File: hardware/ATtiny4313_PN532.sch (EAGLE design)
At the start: 22 parts, among them IC1 ATtiny4313, J2 AVR ISP, Q1 14.7456MHz, U1 PCA9543AD,118, U3 LTC490CN8PBF, U4 LTC490CN8PBF

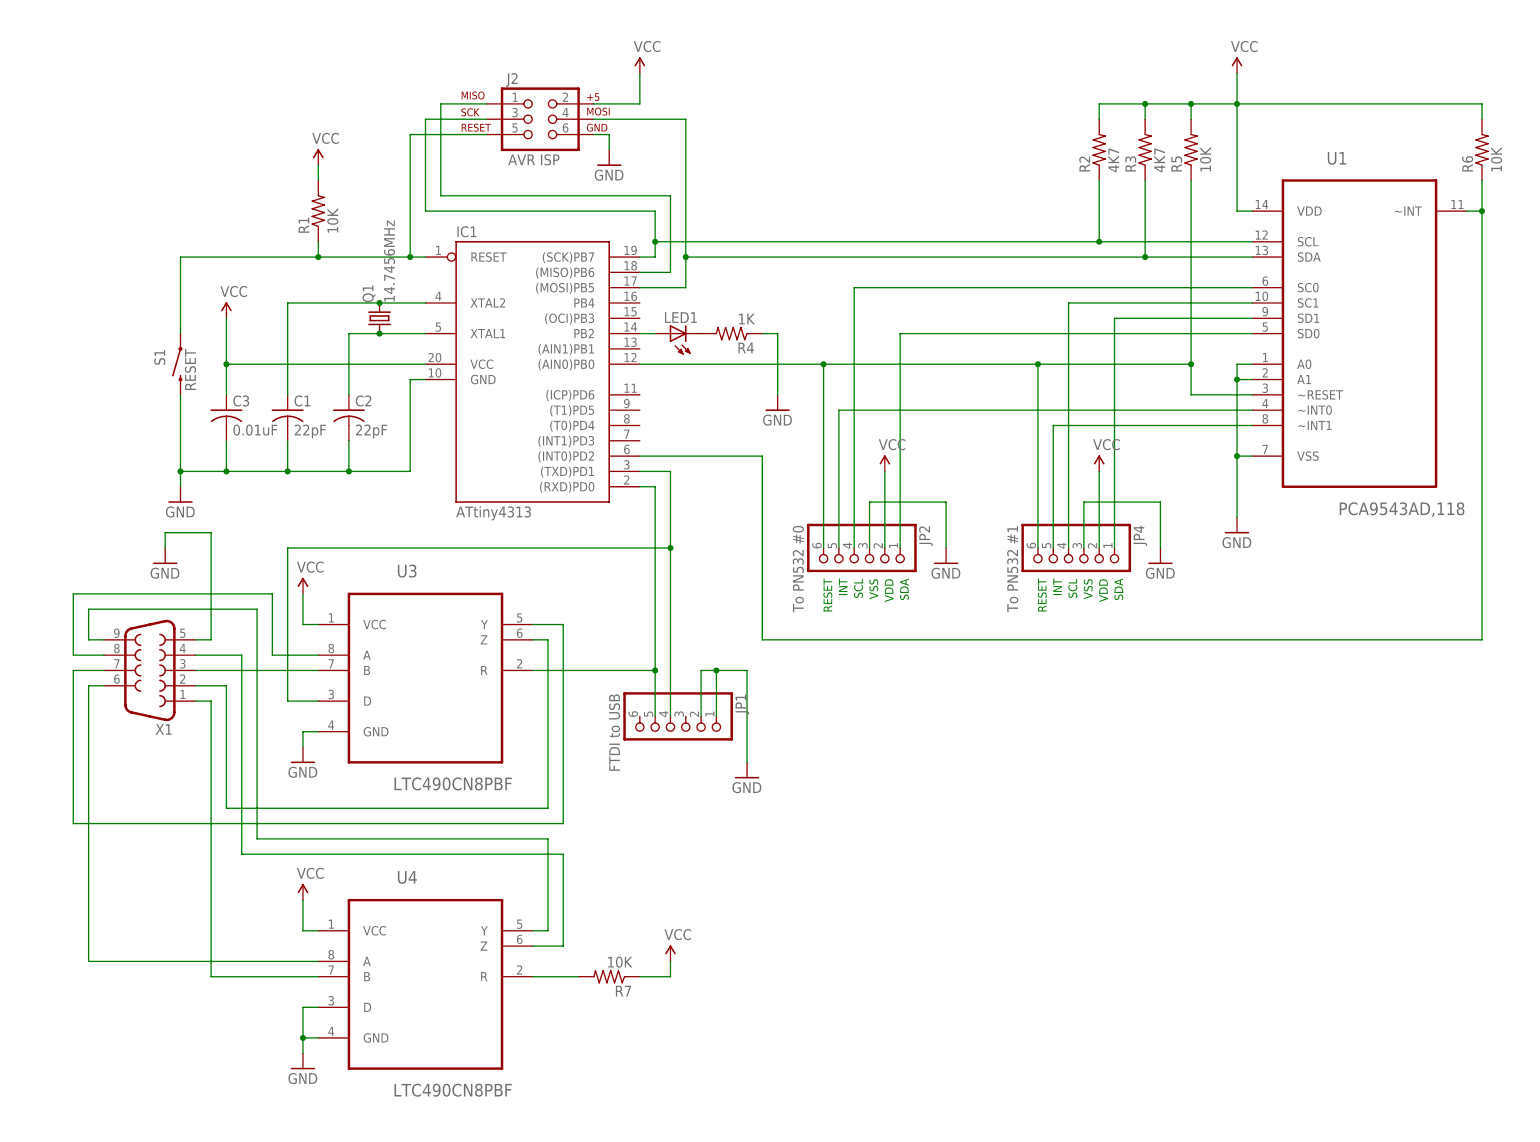
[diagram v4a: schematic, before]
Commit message: Added SDA/SCL isolation switch for programming
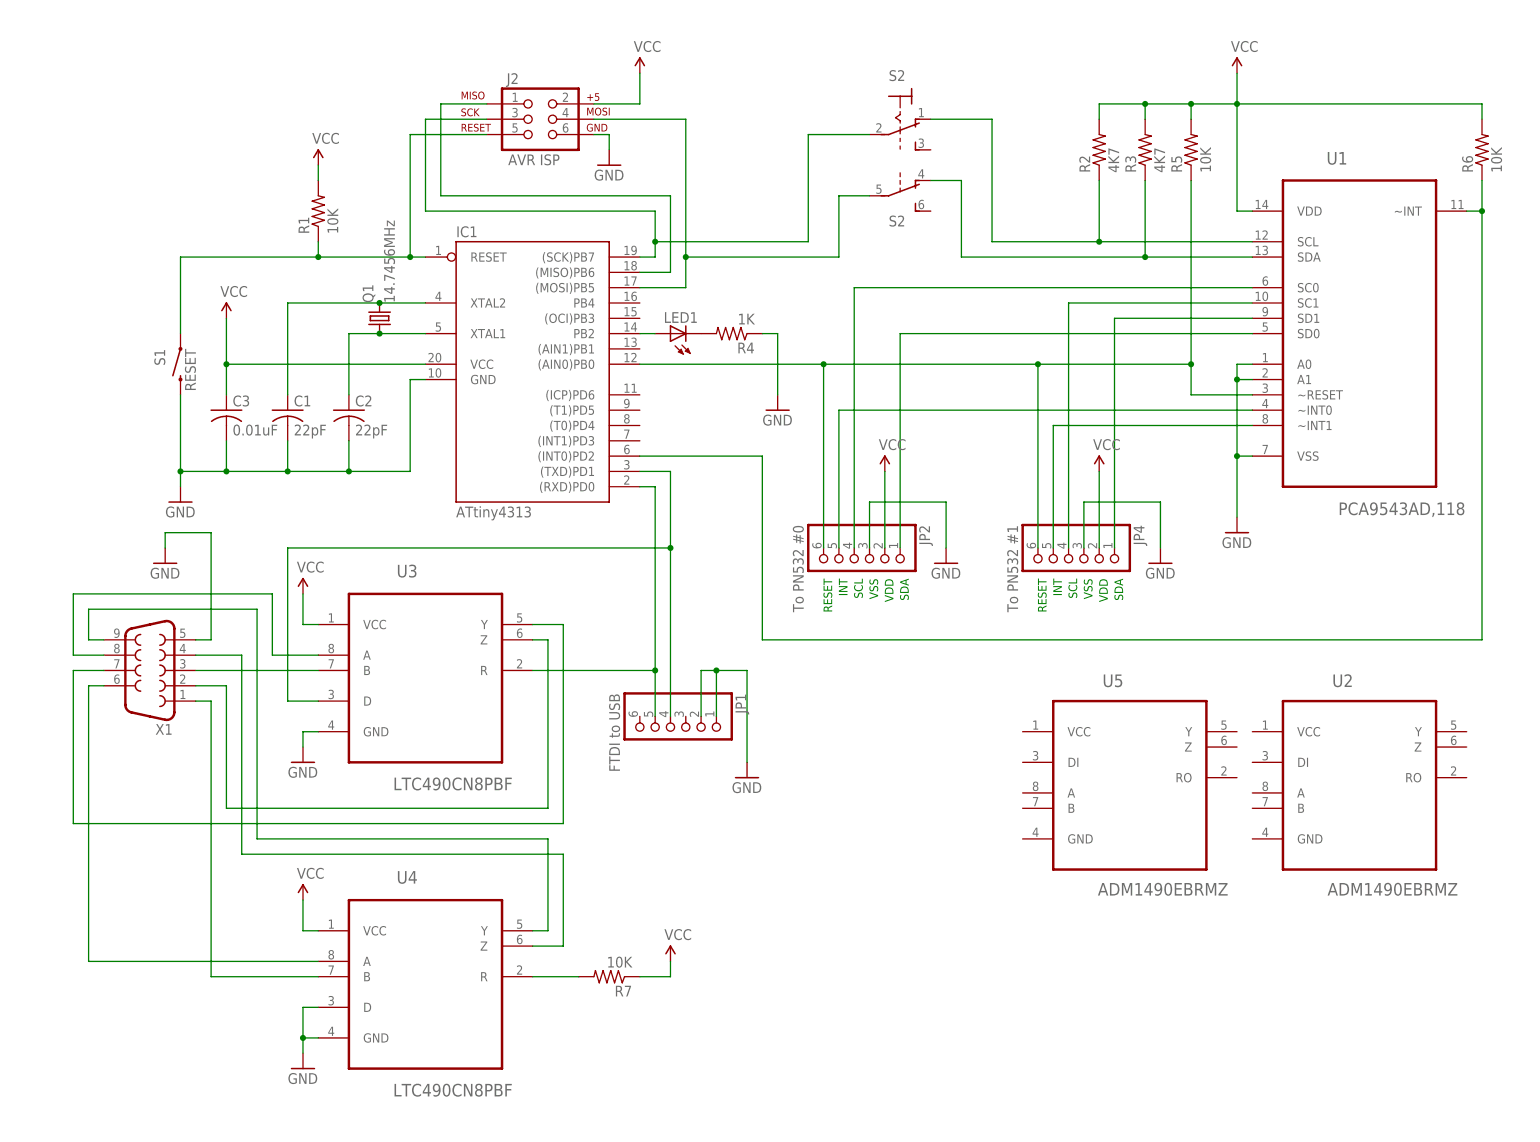
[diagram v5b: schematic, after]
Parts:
- added S2: (no value), switch:320-938
- added U2, U5: ADM1490EBRMZ, Analog Devices_By_element14_Batch_1:ADM1490EBRMZ
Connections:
- new net N$28: R2.1, S21.O, U1.SCL
- new net N$29: R3.1, S2B.O, U1.SDA
- net SCL: now also S21.P; no longer R2.1, U1.SCL
- net SDA: now also S2B.P; no longer R3.1, U1.SDA
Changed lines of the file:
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@@
 <part name="R7" library="rcl" deviceset="R-US_" device="0204/2V" value="10K"/>
 <part name="P+9" library="SparkFun-Aesthetics" deviceset="VCC" device=""/>
+<part name="U2" library="Analog Devices_By_element14_Batch_1" deviceset="ADM1490EBRMZ" device=""/>
+<part name="U5" library="Analog Devices_By_element14_Batch_1" deviceset="ADM1490EBRMZ" device=""/>
+<part name="S2" library="switch" deviceset="320-938" device=""/>
 </parts>
 <sheets>
@@
 <instance part="R7" gate="G$1" x="99.06" y="25.4" rot="R180"/>
 <instance part="P+9" gate="1" x="109.22" y="27.94"/>
+<instance part="U2" gate="A" x="223.52" y="60.96"/>
+<instance part="U5" gate="A" x="185.42" y="60.96"/>
+<instance part="S2" gate="B" x="147.32" y="154.94" rot="R270"/>
+<instance part="S2" gate="1" x="147.32" y="167.64" rot="R270"/>
 </instances>
 <busses>
@@
 <wire x1="106.68" y1="144.78" x2="104.14" y2="144.78" width="0.1524" layer="91"/>
 <pinref part="IC1" gate="G$1" pin="(SCK)PB7"/>
-<wire x1="106.68" y1="147.32" x2="180.34" y2="147.32" width="0.1524" layer="91"/>
+<wire x1="106.68" y1="147.32" x2="132.08" y2="147.32" width="0.1524" layer="91"/>
 <junction x="106.68" y="147.32"/>
-<pinref part="R2" gate="G$1" pin="1"/>
-<wire x1="180.34" y1="157.48" x2="180.34" y2="147.32" width="0.1524" layer="91"/>
-<pinref part="U1" gate="A" pin="SCL"/>
 <wire x1="106.68" y1="152.4" x2="106.68" y2="147.32" width="0.1524" layer="91"/>
-<wire x1="180.34" y1="147.32" x2="205.74" y2="147.32" width="0.1524" layer="91"/>
-<junction x="180.34" y="147.32"/>
 <pinref part="J2" gate="G$1" pin="3"/>
 <wire x1="78.74" y1="167.64" x2="68.58" y2="167.64" width="0.1524" layer="91"/>
 <wire x1="68.58" y1="167.64" x2="68.58" y2="152.4" width="0.1524" layer="91"/>
 <wire x1="68.58" y1="152.4" x2="106.68" y2="152.4" width="0.1524" layer="91"/>
+<pinref part="S2" gate="1" pin="P"/>
+<wire x1="142.24" y1="165.1" x2="132.08" y2="165.1" width="0.1524" layer="91"/>
+<wire x1="132.08" y1="165.1" x2="132.08" y2="147.32" width="0.1524" layer="91"/>
 </segment>
 </net>
@@
 <wire x1="111.76" y1="144.78" x2="111.76" y2="139.7" width="0.1524" layer="91"/>
 <wire x1="111.76" y1="139.7" x2="104.14" y2="139.7" width="0.1524" layer="91"/>
-<wire x1="111.76" y1="144.78" x2="187.96" y2="144.78" width="0.1524" layer="91"/>
+<wire x1="111.76" y1="144.78" x2="137.16" y2="144.78" width="0.1524" layer="91"/>
 <junction x="111.76" y="144.78"/>
-<pinref part="R3" gate="G$1" pin="1"/>
-<wire x1="187.96" y1="157.48" x2="187.96" y2="144.78" width="0.1524" layer="91"/>
 <pinref part="J2" gate="G$1" pin="4"/>
 <wire x1="96.52" y1="167.64" x2="111.76" y2="167.64" width="0.1524" layer="91"/>
-<pinref part="U1" gate="A" pin="SDA"/>
-<wire x1="187.96" y1="144.78" x2="205.74" y2="144.78" width="0.1524" layer="91"/>
-<junction x="187.96" y="144.78"/>
+<pinref part="S2" gate="B" pin="P"/>
+<wire x1="142.24" y1="154.94" x2="137.16" y2="154.94" width="0.1524" layer="91"/>
+<wire x1="137.16" y1="154.94" x2="137.16" y2="144.78" width="0.1524" layer="91"/>
 </segment>
 </net>
@@
 </segment>
 </net>
+<net name="N$28" class="0">
+<segment>
+<pinref part="U1" gate="A" pin="SCL"/>
+<pinref part="R2" gate="G$1" pin="1"/>
+<wire x1="180.34" y1="157.48" x2="180.34" y2="147.32" width="0.1524" layer="91"/>
+<wire x1="180.34" y1="147.32" x2="205.74" y2="147.32" width="0.1524" layer="91"/>
+<junction x="180.34" y="147.32"/>
+<wire x1="162.56" y1="147.32" x2="180.34" y2="147.32" width="0.1524" layer="91"/>
+<pinref part="S2" gate="1" pin="O"/>
+<wire x1="152.4" y1="167.64" x2="162.56" y2="167.64" width="0.1524" layer="91"/>
+<wire x1="162.56" y1="167.64" x2="162.56" y2="147.32" width="0.1524" layer="91"/>
+</segment>
+</net>
+<net name="N$29" class="0">
+<segment>
+<pinref part="U1" gate="A" pin="SDA"/>
+<pinref part="R3" gate="G$1" pin="1"/>
+<wire x1="187.96" y1="157.48" x2="187.96" y2="144.78" width="0.1524" layer="91"/>
+<wire x1="187.96" y1="144.78" x2="205.74" y2="144.78" width="0.1524" layer="91"/>
+<junction x="187.96" y="144.78"/>
+<wire x1="157.48" y1="144.78" x2="187.96" y2="144.78" width="0.1524" layer="91"/>
+<pinref part="S2" gate="B" pin="O"/>
+<wire x1="152.4" y1="157.48" x2="157.48" y2="157.48" width="0.1524" layer="91"/>
+<wire x1="157.48" y1="157.48" x2="157.48" y2="144.78" width="0.1524" layer="91"/>
+</segment>
+</net>

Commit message: Swapped in ADM1490 RS422 xcvr, removed led
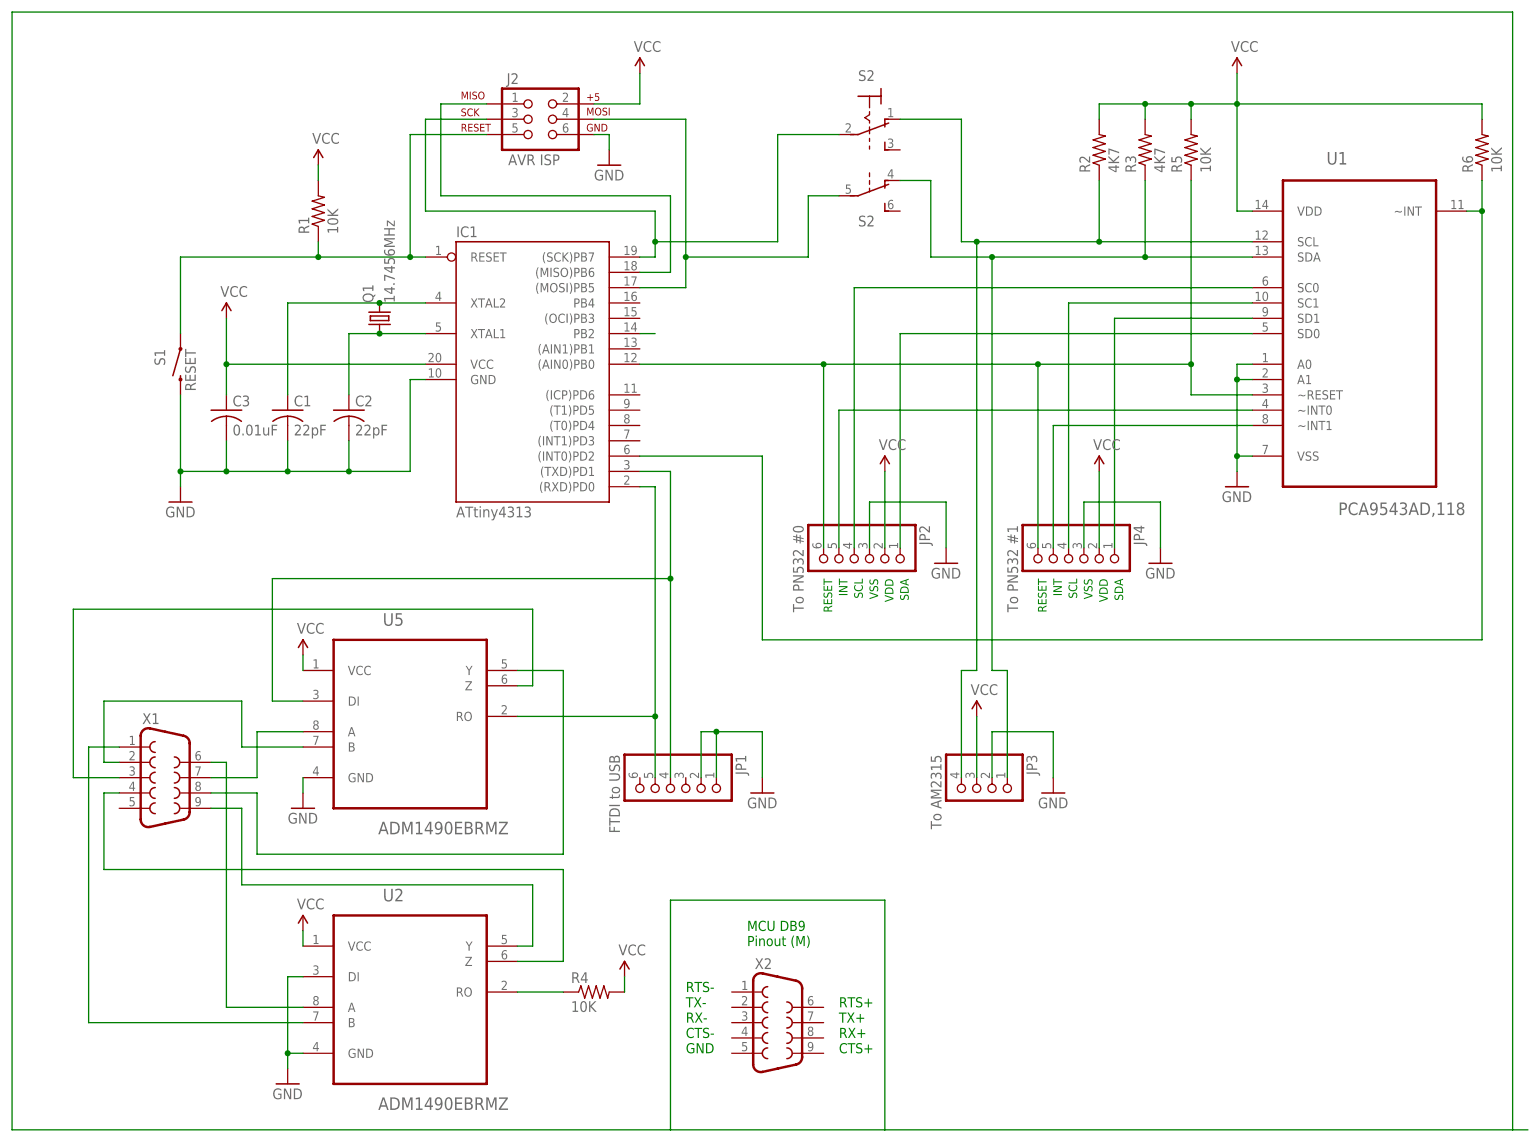
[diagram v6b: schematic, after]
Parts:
- removed LED1: (no value), adafruit:LED5MM
- removed R7: 10K, rcl:R-US_0204/2V
- removed U3, U4: LTC490CN8PBF, LTC_By_element14_Batch_1:LTC490CN8PBF
- added JP3: To AM2315, pinhead:PINHD-1X4/90
- added X2: (no value), SparkFun-Connectors:DB9MALE
- R4: value 1K -> 10K
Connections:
- removed net N$25: U4.A, X1.6
- removed net N$26: U4.Z, X1.4
- removed net N$27: U4.Y, X1.9
- new net N$17: U5.A, X1.7
- new net N$23: U2.A, X1.6
- net GND: now also JP3.2, U2.DI, U2.GND, U5.GND; no longer R4.1, U3.GND, U4.D, U4.GND, X1.5
- net N$19: now also U5.B, X1.2; no longer U3.B, X1.3
- net N$20: now also U2.Y, X1.9; no longer U3.A, X1.8
- net N$21: now also U5.Y, X1.8; no longer U3.Z, X1.2
- net N$22: now also U2.Z, X1.4; no longer U3.Y, X1.7
- net N$24: now also U2.B; no longer U4.B
- net N$28: now also JP3.4
- net N$29: now also JP3.1
- net N$3: now also U5.DI; no longer U3.D
- net N$4: now also U5.RO; no longer U3.R
- net N$5: now also U5.Z, X1.3; no longer R7.2, U4.R
- net N$7: now also R4.1, U2.RO; no longer LED1.C, R4.2
- net N$9: no longer LED1.A
- net VCC: now also JP3.3, R4.2, U2.VCC, U5.VCC; no longer R7.1, U3.VCC, U4.VCC
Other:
- note added: "CTS+"
- note added: "CTS-"
- note added: "GND"
- note added: "MCU DB9 Pinout (M)"
- note added: "RTS+"
- note added: "RTS-"
- note added: "RX+"
- note added: "RX-"
- note added: "TX+"
- note added: "TX-"
- moved on the sheet: JP1, R4, S2, U2, U5, X1
